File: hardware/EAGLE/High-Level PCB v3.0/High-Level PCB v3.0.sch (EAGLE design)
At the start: 56 parts, among them IC1 MCP2551, IC2 DS8921, IC3 DS8921, J1 Optical Mouse, J2 RaspπUart, J8 DB9 Plug, J9 CAN Output, U1 COMPASS, U2 LLSHIFTER, U3 GPS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

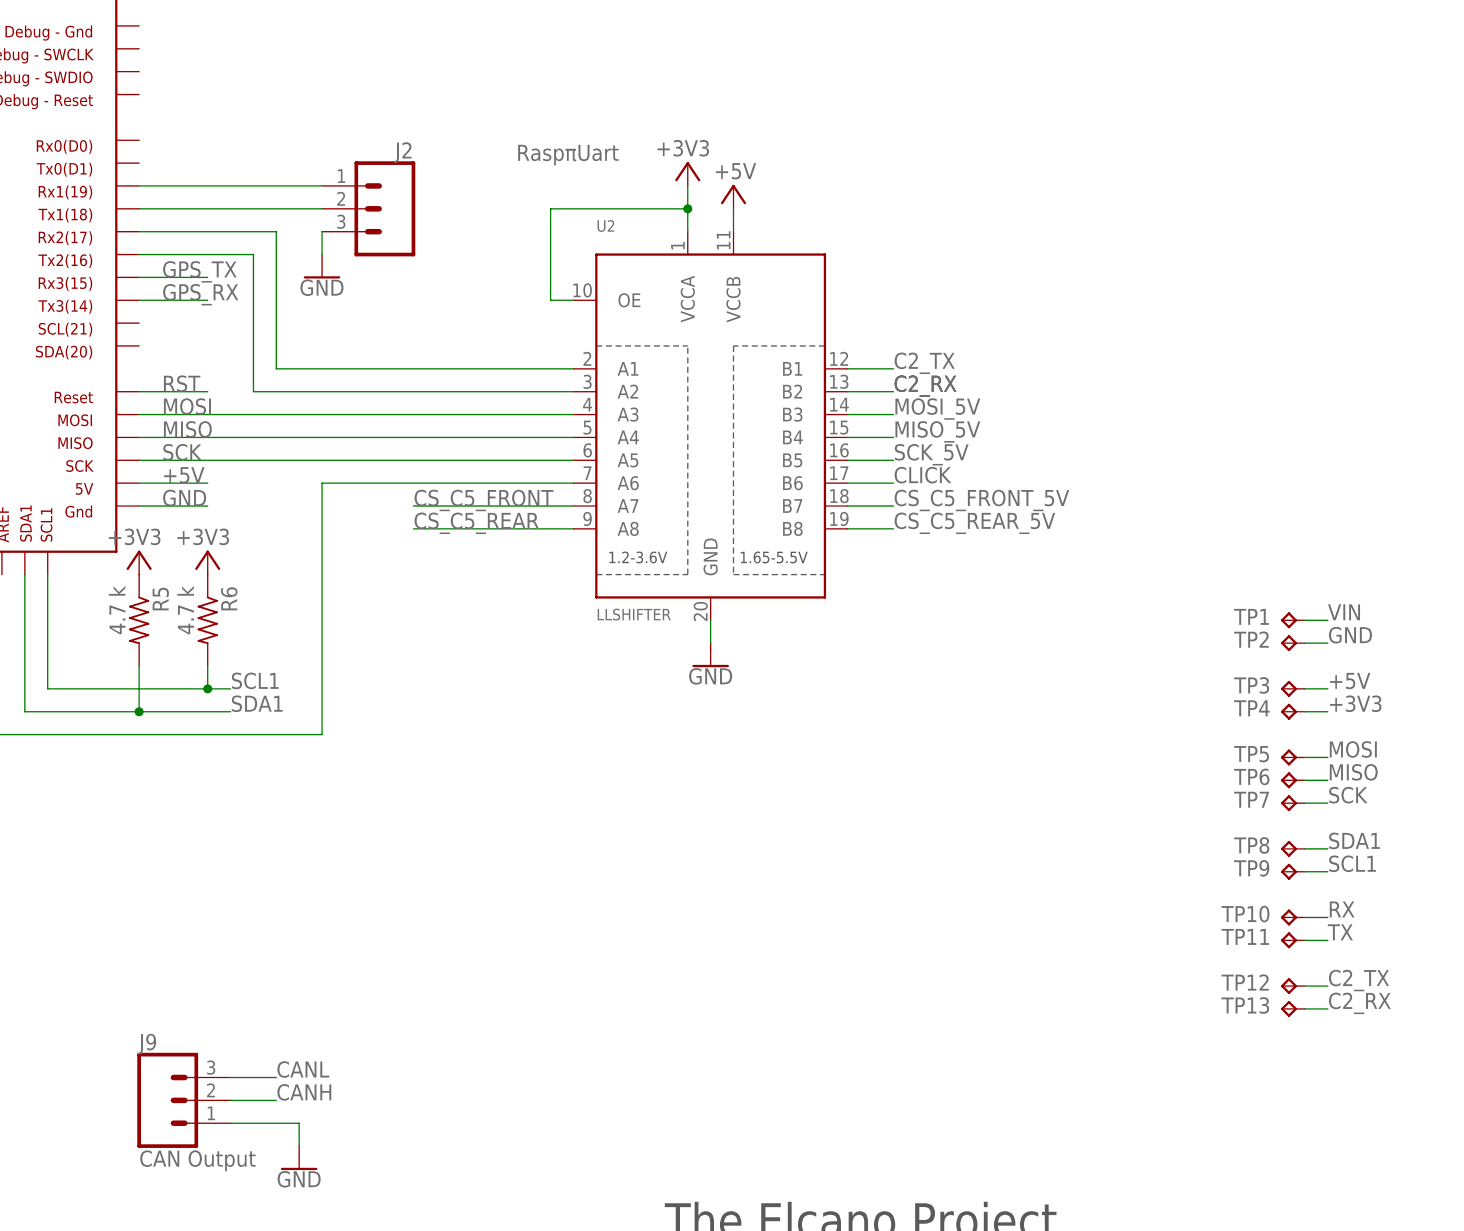
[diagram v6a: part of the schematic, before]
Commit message: Added Board and fixed Test Points
Added the BRD file and fixed GPS test points and added test points for Raspberry UART
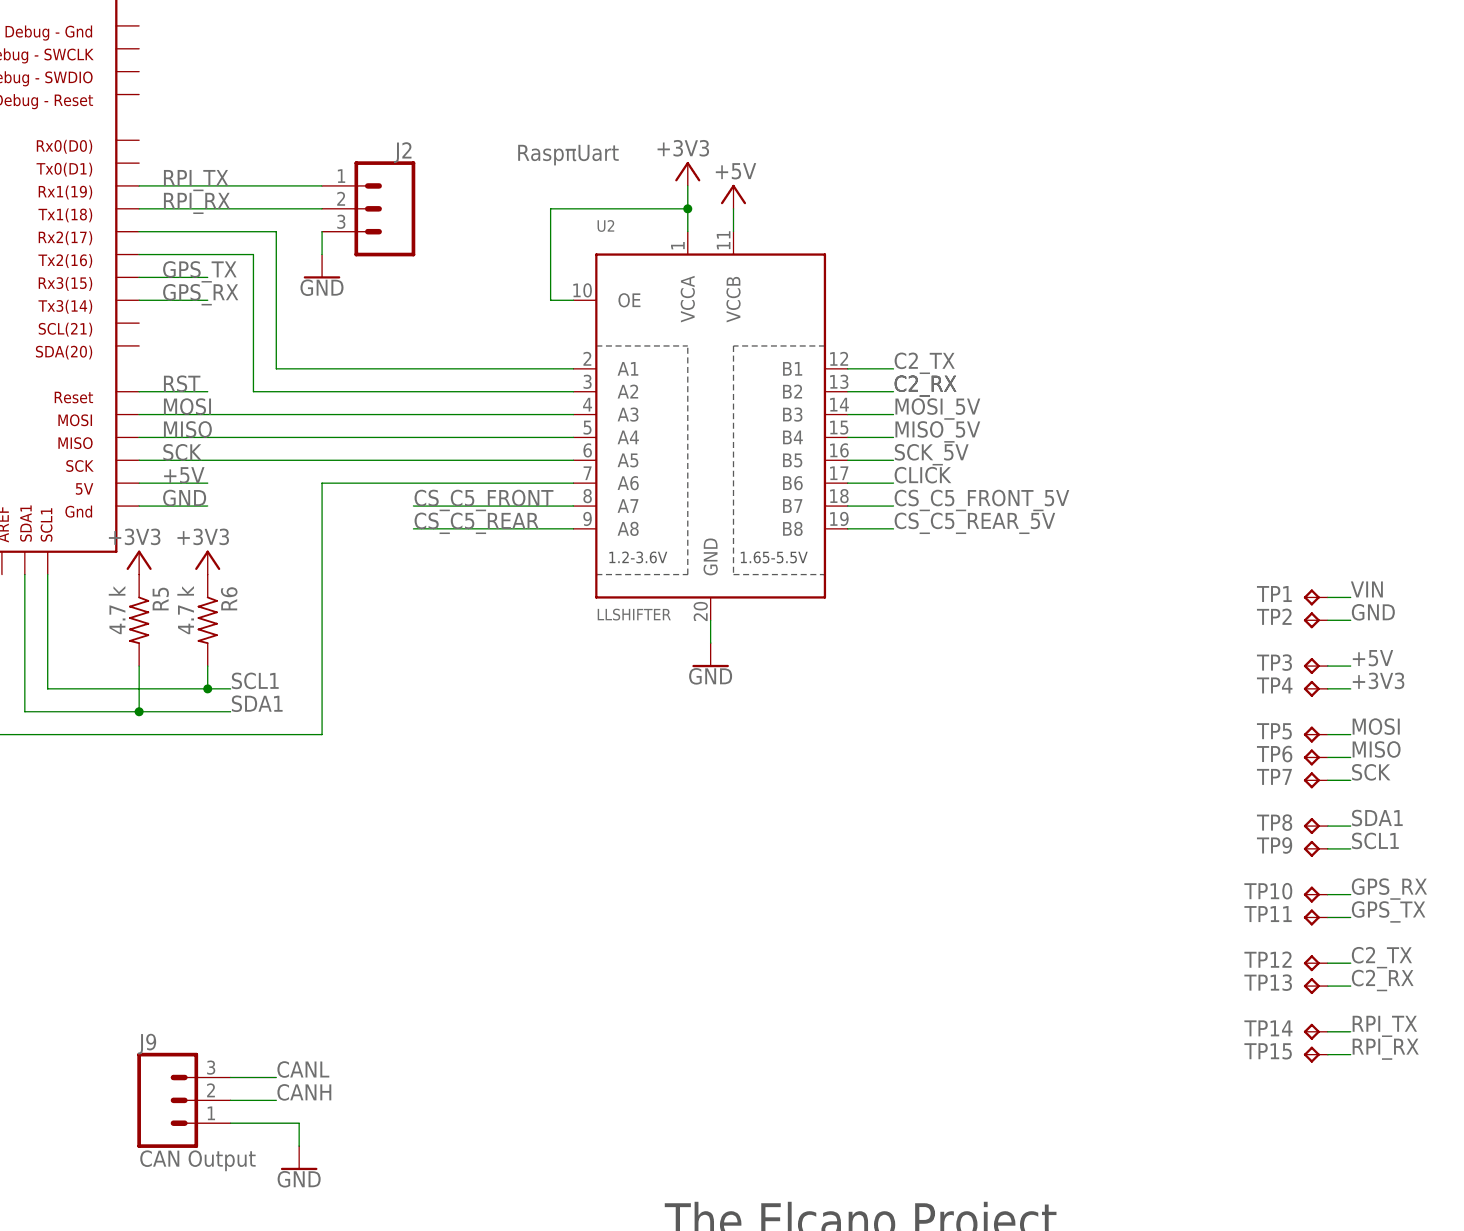
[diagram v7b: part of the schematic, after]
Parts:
- added TP14, TP15: TPPAD1-17, testpad:TPPAD1-17
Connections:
- removed net N$23: J2.2, MCU2.RX1
- removed net N$24: J2.1, MCU2.TX1
- removed net RX: TP10.TP
- removed net TX: TP11.TP
- new net RPI_RX: J2.1, MCU2.TX1, TP15.TP
- new net RPI_TX: J2.2, MCU2.RX1, TP14.TP
- net GPS_RX: now also TP10.TP
- net GPS_TX: now also TP11.TP
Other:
- moved on the sheet: TP1, TP10, TP11, TP12, TP13, TP2, TP3, TP4, TP5, TP6, TP7, TP8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
